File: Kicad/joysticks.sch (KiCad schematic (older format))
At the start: 1 part

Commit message: Completed Audio sheet.
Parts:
- gave numbers to parts that had none: 1
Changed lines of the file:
@@
 Sheet 9 9
 Title ""
-Date ""
+Date "2020-12-20"
 Rev ""
-Comp ""
-Comment1 ""
-Comment2 ""
+Comp "https://neotron-compute.github.io/"
+Comment1 "Licenced as CC BY-SA"
+Comment2 "Copyright (c) The Neotron Developers, 2020"
 Comment3 ""
 Comment4 ""
 $EndDescr
 $Comp
-L Connector:DB9_Female_MountingHoles J?
+L Connector:DB9_Female_MountingHoles J901
 U 1 1 5FDF5DC1
 P 3100 2900
-F 0 "J?" V 3417 2856 50  0000 C CNN
+F 0 "J901" V 3417 2856 50  0000 C CNN
 F 1 "DB9_Female_MountingHoles" V 3326 2856 50  0000 C CNN
 F 2 "" H 3100 2900 50  0001 C CNN

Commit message: Dummy change
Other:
- note added: "FOO Atari/Commodore digital joystick interface.\nCan support SEGA MegaDrive/Genesis pads if\nyou put 5V on Pin 5, and a Select signal on pin 7.\n\nYou can also use an IDC 10-way box header along with\nan IDC 9-way socket on a ribbon. If so, Pin 10 is N/C."
- note removed: "Atari/Commodore digital joystick interface.\nCan support SEGA MegaDrive/Genesis pads if\nyou put 5V on Pin 5, and a Select signal on pin 7.\n\nYou can also use an IDC 10-way box header along with\nan IDC 9-way socket on a ribbon. If so, Pin 10 is N/C."
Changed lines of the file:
@@
 $EndComp
 Text Notes 3850 3150 0    50   ~ 0
-Atari/Commodore digital joystick interface.\nCan support SEGA MegaDrive/Genesis pads if\nyou put 5V on Pin 5, and a Select signal on pin 7.\n\nYou can also use an IDC 10-way box header along with\nan IDC 9-way socket on a ribbon. If so, Pin 10 is N/C.
+FOO Atari/Commodore digital joystick interface.\nCan support SEGA MegaDrive/Genesis pads if\nyou put 5V on Pin 5, and a Select signal on pin 7.\n\nYou can also use an IDC 10-way box header along with\nan IDC 9-way socket on a ribbon. If so, Pin 10 is N/C.
 $EndSCHEMATC

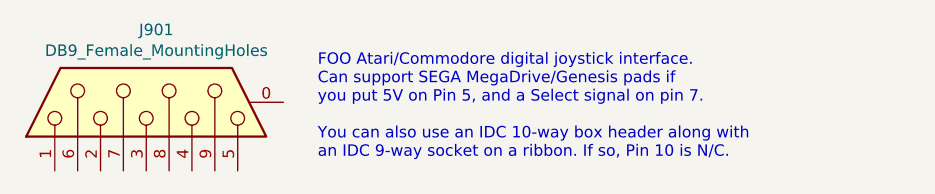
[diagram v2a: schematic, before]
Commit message: Need to touch an sch to get it to build.
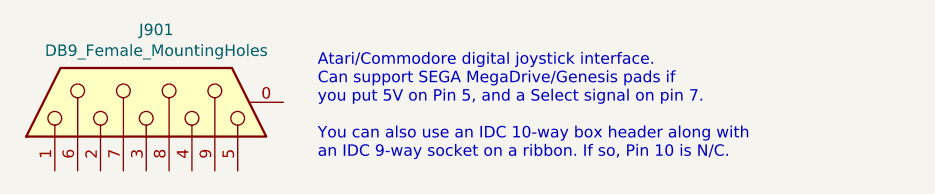
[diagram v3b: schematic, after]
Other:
- note added: "Atari/Commodore digital joystick interface.\nCan support SEGA MegaDrive/Genesis pads if\nyou put 5V on Pin 5, and a Select signal on pin 7.\n\nYou can also use an IDC 10-way box header along with\nan IDC 9-way socket on a ribbon. If so, Pin 10 is N/C."
- note removed: "FOO Atari/Commodore digital joystick interface.\nCan support SEGA MegaDrive/Genesis pads if\nyou put 5V on Pin 5, and a Select signal on pin 7.\n\nYou can also use an IDC 10-way box header along with\nan IDC 9-way socket on a ribbon. If so, Pin 10 is N/C."
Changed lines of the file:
@@
 $EndComp
 Text Notes 3850 3150 0    50   ~ 0
-FOO Atari/Commodore digital joystick interface.\nCan support SEGA MegaDrive/Genesis pads if\nyou put 5V on Pin 5, and a Select signal on pin 7.\n\nYou can also use an IDC 10-way box header along with\nan IDC 9-way socket on a ribbon. If so, Pin 10 is N/C.
+Atari/Commodore digital joystick interface.\nCan support SEGA MegaDrive/Genesis pads if\nyou put 5V on Pin 5, and a Select signal on pin 7.\n\nYou can also use an IDC 10-way box header along with\nan IDC 9-way socket on a ribbon. If so, Pin 10 is N/C.
 $EndSCHEMATC

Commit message: Brought in RS232 circuit from Neotron 32.
Also updated 3D models.
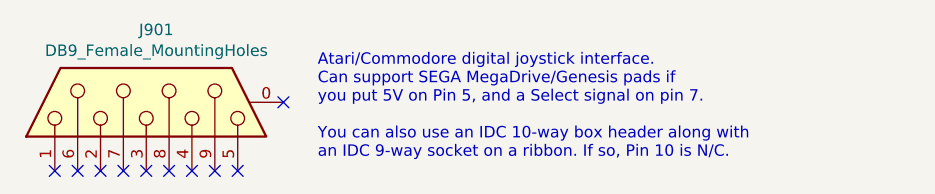
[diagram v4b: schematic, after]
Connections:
- no-connect marks 0 -> 10
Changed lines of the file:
@@
 Text Notes 3850 3150 0    50   ~ 0
 Atari/Commodore digital joystick interface.\nCan support SEGA MegaDrive/Genesis pads if\nyou put 5V on Pin 5, and a Select signal on pin 7.\n\nYou can also use an IDC 10-way box header along with\nan IDC 9-way socket on a ribbon. If so, Pin 10 is N/C.
+NoConn ~ 2700 3200
+NoConn ~ 2800 3200
+NoConn ~ 2900 3200
+NoConn ~ 3000 3200
+NoConn ~ 3100 3200
+NoConn ~ 3200 3200
+NoConn ~ 3300 3200
+NoConn ~ 3400 3200
+NoConn ~ 3500 3200
+NoConn ~ 3700 2900
 $EndSCHEMATC

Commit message: Updating BOM with parts.
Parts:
- J901: footprint (none) -> Connector_Dsub:DSUB-9_Female_Horizontal_P2.77x2.84mm_EdgePinOffset4.94mm_Housed_MountingHolesOffset7.48mm; DNP (none) -> 0
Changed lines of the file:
@@
 F 0 "J901" V 3417 2856 50  0000 C CNN
 F 1 "DB9_Female_MountingHoles" V 3326 2856 50  0000 C CNN
-F 2 "" H 3100 2900 50  0001 C CNN
+F 2 "Connector_Dsub:DSUB-9_Female_Horizontal_P2.77x2.84mm_EdgePinOffset4.94mm_Housed_MountingHolesOffset7.48mm" H 3100 2900 50  0001 C CNN
 F 3 " ~" H 3100 2900 50  0001 C CNN
+F 4 "0" H 3100 2900 50  0001 C CNN "DNP"
 	1    3100 2900
 	0    -1   -1   0
